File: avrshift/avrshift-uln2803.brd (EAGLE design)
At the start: 49.2 x 49.5 mm, 33 parts, among them IC1 AT90S2313P, IC2 7805TV, IC3 ULN2803A, IC4 ULN2803A

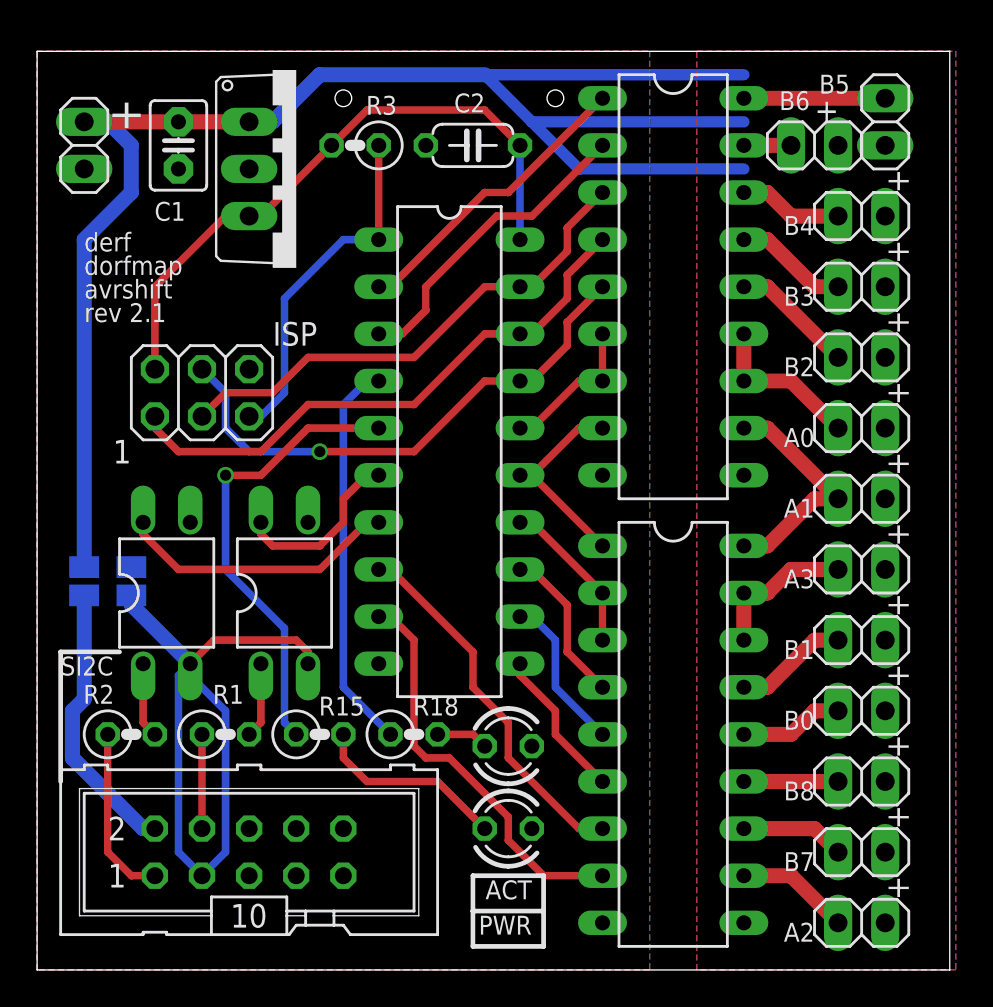
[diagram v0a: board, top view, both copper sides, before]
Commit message: avrshift: Add labels for avrmf pins, extend VCC net to 7805 and input
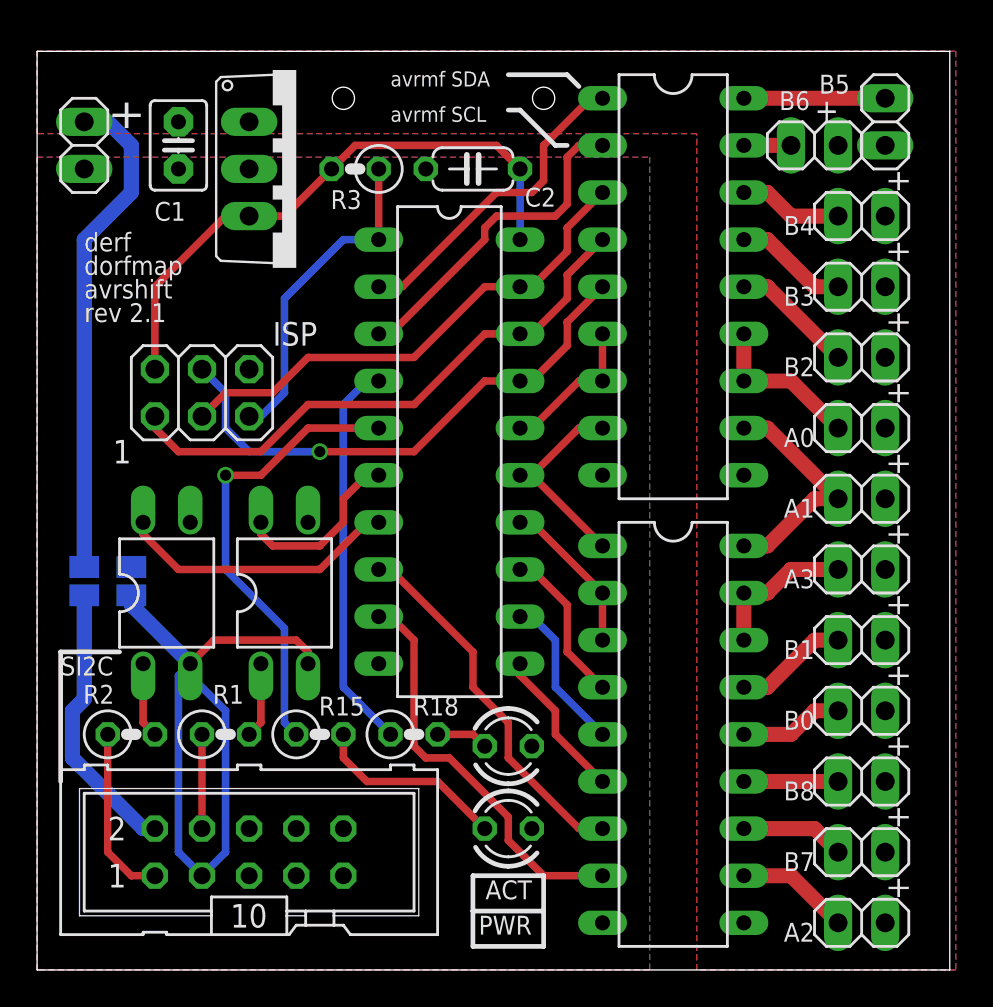
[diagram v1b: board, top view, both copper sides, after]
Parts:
- moved C2 1.27 mm to (23.5, 43.2)
- moved R3 1.27 mm to (17.1, 43.2)
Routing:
- net VCC: track 91.0 -> 26.9 mm
- net 5V: track 33.9 -> 31.6 mm
- net RST: track 19.0 -> 17.7 mm
- net AVRO02: track 17.0 -> 18.1 mm
- net AVRO01: track 16.3 -> 17.4 mm
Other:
- board text added: "avrmf SCL"
- board text added: "avrmf SDA"
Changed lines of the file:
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@@
 <text x="43.815" y="48.26" size="1.016" layer="25" font="vector" rot="R180">B5</text>
 <text x="40.005" y="46.355" size="1.016" layer="25" font="vector">B6</text>
-<hole x="27.94" y="46.99" drill="0.9"/>
-<hole x="16.51" y="46.99" drill="0.9"/>
+<hole x="27.305" y="46.99" drill="1.2"/>
+<hole x="16.51" y="46.99" drill="1.2"/>
 <text x="2.54" y="37.465" size="1.016" layer="25" font="vector">dorfmap</text>
 <text x="2.54" y="36.195" size="1.016" layer="25" font="vector">avrshift</text>
@@
 <wire x1="23.495" y1="3.175" x2="23.495" y2="5.08" width="0.254" layer="25"/>
 <wire x1="23.495" y1="3.175" x2="27.305" y2="3.175" width="0.254" layer="25"/>
+<text x="19.05" y="47.625" size="0.8128" layer="25">avrmf SDA</text>
+<text x="19.05" y="45.72" size="0.8128" layer="25">avrmf SCL</text>
+<wire x1="25.4" y1="48.26" x2="28.575" y2="48.26" width="0.254" layer="25"/>
+<wire x1="28.575" y1="48.26" x2="29.21" y2="47.625" width="0.254" layer="25"/>
+<wire x1="25.4" y1="46.355" x2="26.035" y2="46.355" width="0.254" layer="25"/>
+<wire x1="26.035" y1="46.355" x2="27.94" y2="44.45" width="0.254" layer="25"/>
+<wire x1="27.94" y1="44.45" x2="28.575" y2="44.45" width="0.254" layer="25"/>
 </plain>
 <attributes>
@@
 <attribute name="VALUE" x="4.572" y="46.101" size="1.27" layer="27" ratio="10" rot="R270"/>
 </element>
-<element name="C2" library="rcl" package="C050-024X044" value="100nF" x="23.495" y="44.45" smashed="yes" rot="R180">
-<attribute name="NAME" x="22.479" y="46.228" size="1.016" layer="25" font="vector" ratio="10"/>
-<attribute name="VALUE" x="25.146" y="47.498" size="1.27" layer="27" ratio="10" rot="R180"/>
+<element name="C2" library="rcl" package="C050-024X044" value="100nF" x="23.495" y="43.18" smashed="yes" rot="R180">
+<attribute name="NAME" x="26.289" y="41.148" size="1.016" layer="25" font="vector" ratio="10"/>
+<attribute name="VALUE" x="25.146" y="46.228" size="1.27" layer="27" ratio="10" rot="R180"/>
 </element>
 <element name="SJ1" library="jumper" package="SJ" value="BUSPWR" x="2.54" y="20.955" smashed="yes" rot="MR270">
@@
 <attribute name="VALUE" x="5.08" y="20.5549" size="0.02" layer="28" rot="MR270"/>
 </element>
-<element name="R3" library="rcl" package="0207/2V" value="10K" x="17.145" y="44.45" smashed="yes" rot="R180">
-<attribute name="NAME" x="17.7292" y="46.101" size="1.016" layer="25" font="vector" ratio="10"/>
-<attribute name="VALUE" x="17.1958" y="46.6852" size="1.27" layer="27" ratio="10" rot="R180"/>
+<element name="R3" library="rcl" package="0207/2V" value="10K" x="17.145" y="43.18" smashed="yes" rot="R180">
+<attribute name="NAME" x="15.8242" y="41.021" size="1.016" layer="25" font="vector" ratio="10"/>
+<attribute name="VALUE" x="17.1958" y="45.4152" size="1.27" layer="27" ratio="10" rot="R180"/>
 </element>
 <element name="R15" library="rcl" package="0207/2V" value="470" x="15.24" y="12.7" smashed="yes">
@@
 <contactref element="JP1" pad="1"/>
 <polygon width="0.4064" layer="1" isolate="0.3048">
-<vertex x="0" y="49.53"/>
-<vertex x="33.02" y="49.53"/>
+<vertex x="0" y="43.815"/>
+<vertex x="33.02" y="43.815"/>
 <vertex x="33.02" y="0"/>
 <vertex x="0" y="0"/>
@@
 <polygon width="0.4064" layer="16" isolate="0.3048">
 <vertex x="0" y="0"/>
-<vertex x="0" y="49.53"/>
-<vertex x="33.02" y="49.53"/>
+<vertex x="0" y="43.815"/>
+<vertex x="33.02" y="43.815"/>
 <vertex x="33.02" y="0"/>
 </polygon>
@@
 <contactref element="JP10" pad="2"/>
 <contactref element="IC4" pad="10"/>
-<polygon width="0.4064" layer="1" isolate="0.3048">
-<vertex x="35.56" y="49.53"/>
-<vertex x="49.53" y="49.53"/>
-<vertex x="49.53" y="0"/>
-<vertex x="35.56" y="0"/>
-</polygon>
-<polygon width="0.4064" layer="16" isolate="0.3048">
-<vertex x="35.56" y="49.53"/>
-<vertex x="49.53" y="49.53"/>
-<vertex x="49.53" y="0"/>
-<vertex x="35.56" y="0"/>
-</polygon>
-<wire x1="2.54" y1="45.72" x2="7.62" y2="45.72" width="0.8128" layer="1"/>
-<wire x1="7.62" y1="45.72" x2="11.43" y2="45.72" width="0.8128" layer="1"/>
 <wire x1="2.54" y1="45.72" x2="3.81" y2="45.72" width="0.8128" layer="16"/>
 <wire x1="3.81" y1="45.72" x2="5.08" y2="44.45" width="0.8128" layer="16"/>
@@
 <wire x1="5.08" y1="41.91" x2="2.54" y2="39.37" width="0.8128" layer="16"/>
 <wire x1="2.54" y1="39.37" x2="2.54" y2="21.717" width="0.8128" layer="16"/>
-<wire x1="24.13" y1="48.26" x2="38.1" y2="48.26" width="0.6096" layer="16"/>
-<wire x1="26.67" y1="45.72" x2="38.1" y2="45.72" width="0.6096" layer="16"/>
-<wire x1="26.67" y1="45.72" x2="29.21" y2="43.18" width="0.6096" layer="16"/>
-<wire x1="29.21" y1="43.18" x2="38.1" y2="43.18" width="0.6096" layer="16"/>
-<wire x1="15.24" y1="48.26" x2="24.13" y2="48.26" width="0.8128" layer="16"/>
-<wire x1="24.13" y1="48.26" x2="26.67" y2="45.72" width="0.6096" layer="16"/>
-<wire x1="11.43" y1="45.72" x2="12.7" y2="45.72" width="0.8128" layer="16"/>
-<wire x1="12.7" y1="45.72" x2="15.24" y2="48.26" width="0.8128" layer="16"/>
+<polygon width="0.4064" layer="1" isolate="0.3048">
+<vertex x="0" y="49.53"/>
+<vertex x="49.53" y="49.53"/>
+<vertex x="49.53" y="0"/>
+<vertex x="35.56" y="0"/>
+<vertex x="35.56" y="44.45"/>
+<vertex x="35.56" y="45.085"/>
+<vertex x="0" y="45.085"/>
+</polygon>
+<polygon width="0.4064" layer="16" isolate="0.3048">
+<vertex x="0" y="49.53"/>
+<vertex x="49.53" y="49.53"/>
+<vertex x="49.53" y="0"/>
+<vertex x="35.56" y="0"/>
+<vertex x="35.56" y="45.085"/>
+<vertex x="0" y="45.085"/>
+</polygon>
 </signal>
 <signal name="5V">
@@
 <contactref element="C2" pad="1"/>
 <contactref element="IC1" pad="20"/>
-<wire x1="26.035" y1="44.45" x2="26.035" y2="39.37" width="0.4064" layer="16"/>
-<wire x1="11.43" y1="40.64" x2="12.065" y2="40.64" width="0.4064" layer="1"/>
-<wire x1="26.035" y1="44.45" x2="24.13" y2="46.355" width="0.4064" layer="1"/>
-<wire x1="24.13" y1="46.355" x2="17.78" y2="46.355" width="0.4064" layer="1"/>
 <contactref element="SV2" pad="2"/>
 <wire x1="6.35" y1="32.385" x2="6.35" y2="36.83" width="0.4064" layer="1"/>
@@
 <wire x1="10.16" y1="40.64" x2="11.43" y2="40.64" width="0.4064" layer="1"/>
 <contactref element="R3" pad="2"/>
-<wire x1="12.065" y1="40.64" x2="15.875" y2="44.45" width="0.4064" layer="1"/>
-<wire x1="15.875" y1="44.45" x2="17.78" y2="46.355" width="0.4064" layer="1"/>
+<wire x1="11.43" y1="40.64" x2="13.335" y2="40.64" width="0.4064" layer="1"/>
+<wire x1="13.335" y1="40.64" x2="15.875" y2="43.18" width="0.4064" layer="1"/>
+<wire x1="26.035" y1="43.18" x2="24.765" y2="44.45" width="0.4064" layer="1"/>
+<wire x1="24.765" y1="44.45" x2="17.145" y2="44.45" width="0.4064" layer="1"/>
+<wire x1="17.145" y1="44.45" x2="15.875" y2="43.18" width="0.4064" layer="1"/>
+<wire x1="26.035" y1="39.37" x2="26.035" y2="43.18" width="0.4064" layer="16"/>
 </signal>
 <signal name="AVRSDA">
@@
 <wire x1="16.51" y1="39.37" x2="18.415" y2="39.37" width="0.4064" layer="16"/>
 <contactref element="R3" pad="1"/>
-<wire x1="18.415" y1="44.45" x2="18.415" y2="39.37" width="0.4064" layer="1"/>
+<wire x1="18.415" y1="43.18" x2="18.415" y2="39.37" width="0.4064" layer="1"/>
 </signal>
 <signal name="N$21">
@@
 <contactref element="IC1" pad="2"/>
 <contactref element="IC3" pad="1"/>
-<wire x1="18.415" y1="36.83" x2="19.05" y2="36.83" width="0.4064" layer="1"/>
-<wire x1="19.05" y1="36.83" x2="24.13" y2="41.91" width="0.4064" layer="1"/>
-<wire x1="24.13" y1="41.91" x2="25.4" y2="41.91" width="0.4064" layer="1"/>
-<wire x1="25.4" y1="41.91" x2="30.48" y2="46.99" width="0.4064" layer="1"/>
+<wire x1="18.415" y1="36.83" x2="19.685" y2="36.83" width="0.4064" layer="1"/>
+<wire x1="19.685" y1="36.83" x2="24.765" y2="41.91" width="0.4064" layer="1"/>
+<wire x1="24.765" y1="41.91" x2="26.67" y2="41.91" width="0.4064" layer="1"/>
+<wire x1="26.67" y1="41.91" x2="27.305" y2="42.545" width="0.4064" layer="1"/>
+<wire x1="27.305" y1="42.545" x2="27.305" y2="44.45" width="0.4064" layer="1"/>
+<wire x1="27.305" y1="44.45" x2="29.845" y2="46.99" width="0.4064" layer="1"/>
+<wire x1="29.845" y1="46.99" x2="30.48" y2="46.99" width="0.4064" layer="1"/>
 </signal>
 <signal name="AVRO02">
 <contactref element="IC1" pad="3"/>
 <contactref element="IC3" pad="2"/>
-<wire x1="18.415" y1="34.29" x2="19.685" y2="34.29" width="0.4064" layer="1"/>
-<wire x1="19.685" y1="34.29" x2="20.955" y2="35.56" width="0.4064" layer="1"/>
-<wire x1="20.955" y1="35.56" x2="20.955" y2="36.83" width="0.4064" layer="1"/>
-<wire x1="20.955" y1="36.83" x2="24.765" y2="40.64" width="0.4064" layer="1"/>
-<wire x1="24.765" y1="40.64" x2="26.67" y2="40.64" width="0.4064" layer="1"/>
-<wire x1="26.67" y1="40.64" x2="30.48" y2="44.45" width="0.4064" layer="1"/>
+<wire x1="18.415" y1="34.29" x2="19.05" y2="34.29" width="0.4064" layer="1"/>
+<wire x1="19.05" y1="34.29" x2="24.13" y2="39.37" width="0.4064" layer="1"/>
+<wire x1="24.13" y1="39.37" x2="24.13" y2="40.005" width="0.4064" layer="1"/>
+<wire x1="24.13" y1="40.005" x2="24.765" y2="40.64" width="0.4064" layer="1"/>
+<wire x1="24.765" y1="40.64" x2="27.94" y2="40.64" width="0.4064" layer="1"/>
+<wire x1="27.94" y1="40.64" x2="28.575" y2="41.275" width="0.4064" layer="1"/>
+<wire x1="28.575" y1="41.275" x2="28.575" y2="43.815" width="0.4064" layer="1"/>
+<wire x1="28.575" y1="43.815" x2="29.21" y2="44.45" width="0.4064" layer="1"/>
+<wire x1="29.21" y1="44.45" x2="30.48" y2="44.45" width="0.4064" layer="1"/>
 </signal>
 <signal name="AVRO03">
